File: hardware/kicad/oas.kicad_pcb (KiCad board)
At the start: 2 copper layers, 120 x 103.5 mm, 68 parts, among them J1 Phoenix_MSTBA_2,5/3-G-5,08 (2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, J10 Native-USB recovery (DNP), J2 SWD/UART Recovery (DNP), J3 JST SM06B-GHS-TB (SEN66 conne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, J4 1x5 P1.27mm header (HLK-LD241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, J5 ESP32 row A (pins 1..15, ante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, J6 ESP32 row B (pins 16..30, USB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, J7 MIKROE row A (mikroBUS pins 1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, J8 MIKROE row B (mikroBUS pins 9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, J9 JST SM04B-SRSS-TB (Qwiic / St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, Q1 AO3401A, U1 LM2596S-5.0, U2 TPS62933

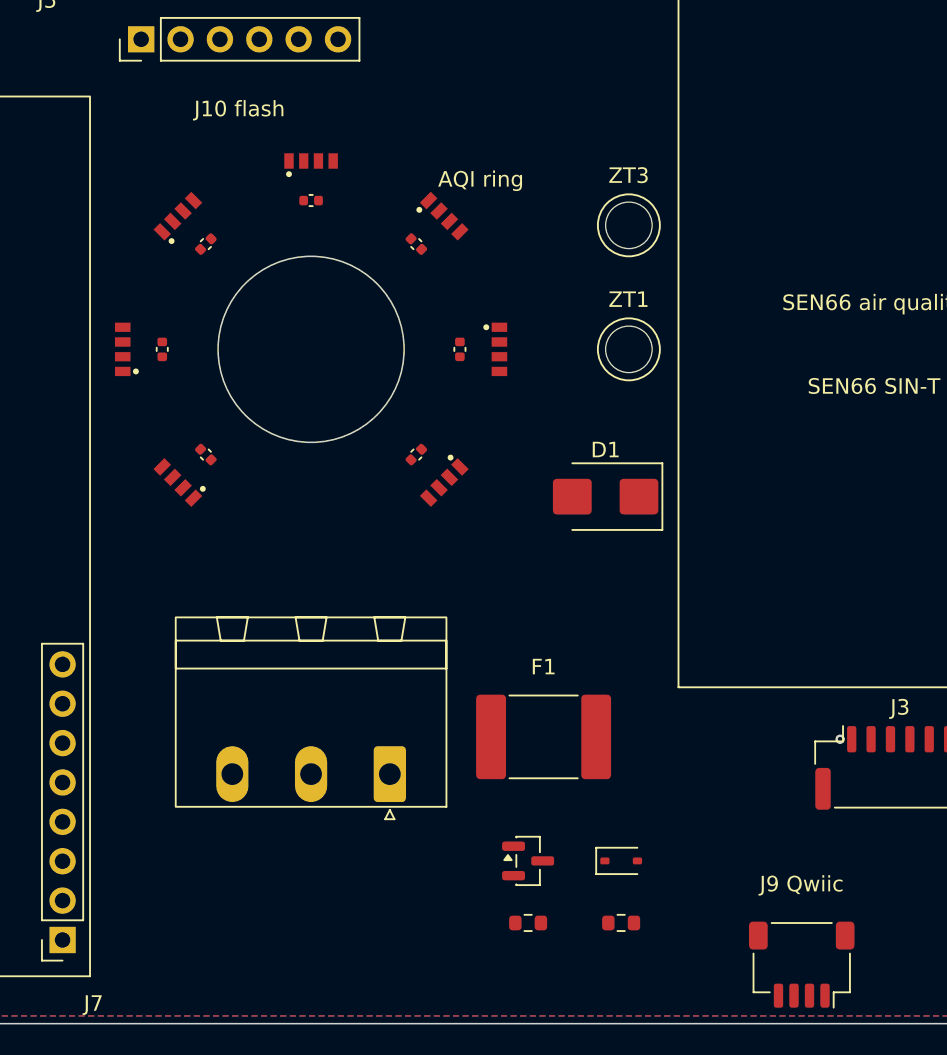
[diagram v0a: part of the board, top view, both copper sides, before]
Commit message: fix(boardgen): LED ring emission outward, F1 1812 downsize, J1 no-go zone
LED ring (SK6812-SIDE D11..D18):
- Flip rotation formula (270-theta) -> (90-theta) so emission face points
  radially OUTWARD from ring centre (was INWARD, hidden under cable hole).
- Bundle 3D STEP model from scottbez1/smartknob (Apache 2.0) so LEDs render
  in 3D. New libraries/oas.3dshapes/ with NOTICE.md for attribution.
- Add show_pin_labels option to gen_sk6812_side_pcb_footprint(); D11 gets
  vertical "Di"/"Gd" silk labels at pads 1/4 for visual orientation check
  during inspection.
- Per-LED radius overrides: D11/D15 R=11 (E-W axis symmetry), D12/D14
  R=16.5 (clear J1 mating plug), C21/C23 cap radial offset 2.6 mm (vs
  3.4 default) so caps sit OUTSIDE J1 plug no-go zone.

J1 (24V Phoenix terminal):
- Rotate Qwiic J9 180->0 (mating face faces south chord opening).
- Shift J1_PCB_Y +5 mm south to widen the plug clearance area.
- Add F.SilkS no-go rectangle (X=±8.73, Y=[+6.4,+21.5]) labelled "J1 PLUG"
  marking the area reserved for the mating plug. Component placement
  ensures nothing lies inside this rect.

F1 polyfuse:
- Downsize 2920 -> 1812 (Littelfuse 1812L075THDR, LCSC C262023) so the
  KiCad-stock R_1812_4532Metric.step can be used as the 3D body (CC-BY-SA
  + Design Exception, commitable to public repo). The stock 2920 footprint
  references a STEP file absent from KiCad 10 install.
- Add model_override parameter to _emit_stock_lib_footprint() helper to
  redirect (model ...) path when stock kicad_mod points at a missing file.

3D renders:
- Add 3 isometric views at 90/180/270 deg azimuth (in addition to existing
  iso = 0 deg) for full 360-deg visual review.

Layout follow-ups (all DRC clean):
- Move "J10 flash" silk text 3 mm south (D17 collision after radius bump).
- Increase MIKROE-2462 height/footprint half-extent entries to cover
  Fuse_1812_4532Metric footprint.
- Remove "AQI ring" board-level silk text (pads of D18 collided with
  the bbox after radius/rotation change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
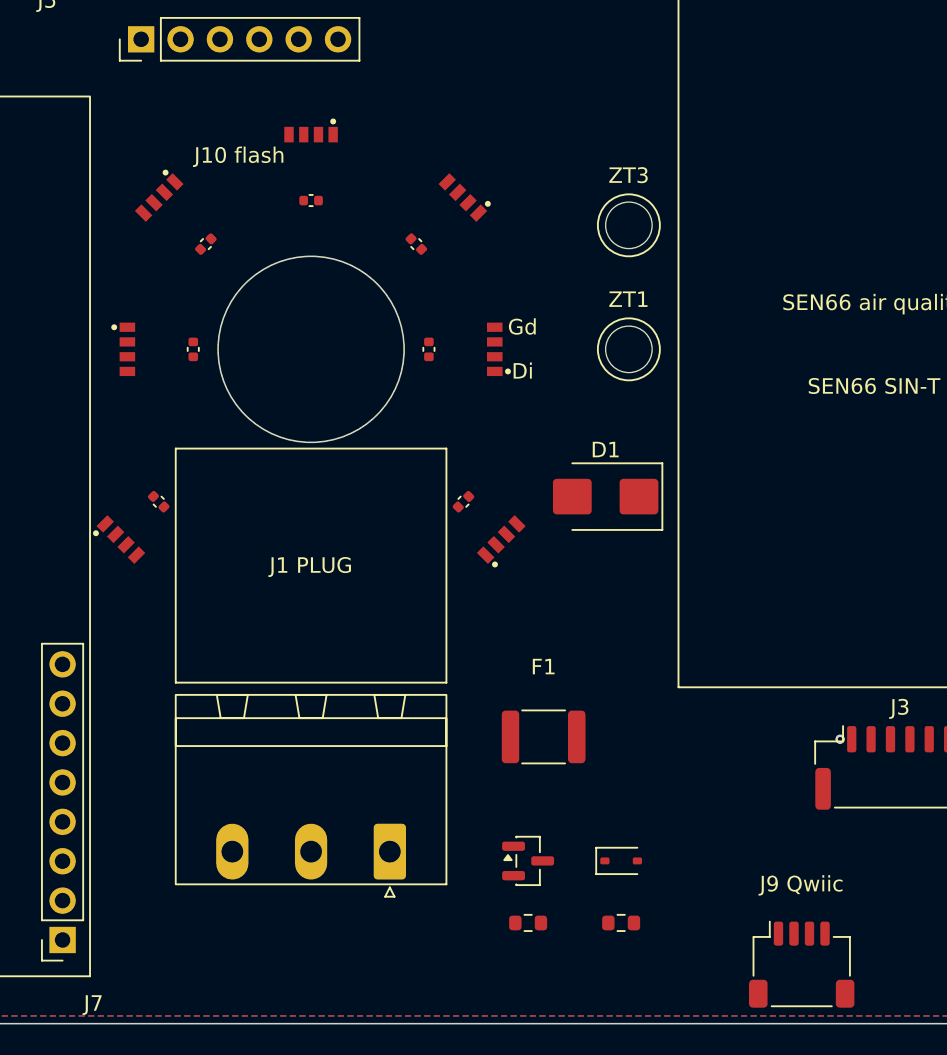
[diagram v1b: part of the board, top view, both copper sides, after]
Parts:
- F1: value MF-RHT075/60-2 -> 1812L075THDR; footprint Fuse:Fuse_2920_7451Metric -> Fuse:Fuse_1812_4532Metric
- moved J1 5.00 mm to (153.6, 137.4)
- moved C21 4.30 mm to (158.3, 114.8), turned to 45 degrees
- moved C23 4.30 mm to (138.7, 114.8), turned to 315 degrees
- moved D12 3.50 mm to (160.2, 116.7), turned to 45 degrees
- moved D14 3.50 mm to (136.8, 116.7), turned to 315 degrees
- moved C20 2.00 mm to (156.1, 105.0), turned to 90 degrees
- moved C24 2.00 mm to (140.9, 105.0), turned to 270 degrees
- moved D11 2.00 mm to (159.5, 105.0), turned to 90 degrees
- moved D15 2.00 mm to (137.5, 105.0), turned to 270 degrees
- turned C25 to 225 degrees
- turned C26 to 180 degrees
- turned C27 to 135 degrees
- turned D16 to 225 degrees
- turned D17 to 180 degrees
- turned D18 to 135 degrees
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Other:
- board text added: "J1 PLUG"
- board text removed: "AQI ring"

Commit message: fix(schematic): C9 non-polarized symbol + J2 label + doc drifts
Closes the remaining items from the 50-agent connectivity audit.

C9 (10 uF MLCC, Samsung CL21A106KAYNNNE — verified ceramic / X5R,
non-polarized) was drawn with Device:C_Polarized, implying a polarity
constraint the part does not have. Switch to Device:C. Connectivity is
unchanged: pin geometry is identical and the +3V3 / GND nets keep
their names.

J2 recovery header was labelled "SWD/UART Recovery" — the ESP32-C6 is
RISC-V and exposes no SWD; the header carries UART + EN + BOOT. Renamed
to "UART/Boot Recovery (DNP)" across BOTH the schematic generator and
the PCB footprint generator (the value string lives in each).

Doc drifts: CLAUDE.md F1 row corrected 2920L075/60MR (C207083) ->
1812L075THDR (C262023) to match the BOM / lcsc_mapping; _sch_mcu.py
GPIO16/17 comments corrected UART0 -> UART1.

29/29 build PASS — DRC 0, ERC 0, determinism OK.

Co-Authored-By: Claude Opus 4.7 <noreply@anthropic.com>
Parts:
- J2: value SWD/UART Recovery (DNP) -> UART/Boot Recovery (DNP)
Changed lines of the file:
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@@
 	(effects (font (size 1 1) (thickness 0.15)))
 )
-(property "Value" "SWD/UART Recovery (DNP)"
+(property "Value" "UART/Boot Recovery (DNP)"
 	(at 2.5 15 0)
 	(layer "F.Fab")

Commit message: fix(boardgen): move J9 to the C2 / RJ45-Ethernet case-wall opening
Physical fit-check of the AK-N-94 enclosure against the manufacturer
DXF showed J9 (Qwiic / Stemma QT) was placed behind a single Ø3.4 mm
round hole — nonsensical for a 4-pin cable connector. Relocate J9 from
the C5 opening to the C2 opening (the RJ45 / Ethernet jack cutout),
centred at PCB X = -8.95. CUTOUTS now emits only the populated C2
keepout zone; the "J9" cutout silk label is shortened and placed in
the silk corridor between the MIKROE NFC body and the J1 terminal block.

Co-Authored-By: Claude Opus 4.7 <noreply@anthropic.com>
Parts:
- moved J9 40.6 mm to (139.6, 144.7)
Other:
- board text added: "C2 15.7×16.3"
- board text added: "J9"
- board text removed: "C5 7.5×6.0"
- board text removed: "J9 Qwiic"
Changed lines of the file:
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@@
 )
 (gr_rect
-	(start 176.4 141.494)
-	(end 183.9 147.494)
+	(start 131.7 132.198)
+	(end 147.4 148.497798)
 	(stroke (width 0.1) (type solid))
 	(fill no)
 	(layer "Dwgs.User")
 )
-(gr_text "C5\n7.5×6.0"
-	(at 180.15 144.494)
+(gr_text "C2\n15.7×16.3"
+	(at 139.55 140.347899)
 	(layer "Dwgs.User")
 	(effects
@@
 (footprint "Connector_JST:JST_SH_SM04B-SRSS-TB_1x04-1MP_P1.00mm_Horizontal"
 	(layer "F.Cu")
-	(at 180.15 144.69 0)
+	(at 139.55 144.69 0)
 (property "Reference" "J9"
 	(at 0 -3.6 0)
@@
 )
 (gr_text "J9 GND"
-	(at 181.65 144.69 0)
+	(at 141.05 144.69 0)
 	(layer "F.Fab")
 	(effects
@@
 	)
 )
-(gr_text "J9 Qwiic"
-	(at 180.15 139.5 0)
+(gr_text "J9"
+	(at 137.64 139.5 0)
 	(layer "F.SilkS")
 	(effects
@@
 	(net_name "")
 	(layers "F.Cu" "B.Cu")
-	(name "Connector_Cutout_C5")
+	(name "Connector_Cutout_C2")
 	(hatch edge 0.508)
 	(connect_pads
@@
 	(polygon
 		(pts
-			(xy 176.4 141.494)
-			(xy 183.9 141.494)
-			(xy 183.9 147.494)
-			(xy 176.4 147.494)
+			(xy 131.7 132.198)
+			(xy 147.4 132.198)
+			(xy 147.4 148.497798)
+			(xy 131.7 148.497798)
 		)
 	)

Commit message: fix(boardgen): mirror J9 / C2 cutout to the +X side
The C2 RJ45 / Ethernet case-wall opening (which hosts the J9 Qwiic /
Stemma QT connector) was transcribed from a bottom-of-enclosure
manufacturer DXF without mirror correction, so it landed on the wrong
(-X / left) side of the board's vertical centerline.

Mirror-correct the C2 cutout X range about X=0 (now +1.1..+16.8),
recentre J9_PCB_X on the cutout midpoint (+8.95), and reposition the
board-level "J9" F.SilkS label into the clear silk corridor on the
+X side. Comments updated to reflect the bottom-view DXF correction.

Co-Authored-By: Claude Opus 4.7 <noreply@anthropic.com>
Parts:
- moved J9 17.9 mm to (157.4, 144.7)
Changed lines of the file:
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@@
 )
 (gr_rect
-	(start 131.7 132.198)
-	(end 147.4 148.497798)
+	(start 149.6 132.198)
+	(end 165.3 148.497798)
 	(stroke (width 0.1) (type solid))
 	(fill no)
@@
 )
 (gr_text "C2\n15.7×16.3"
-	(at 139.55 140.347899)
+	(at 157.45 140.347899)
 	(layer "Dwgs.User")
 	(effects
@@
 (footprint "Connector_JST:JST_SH_SM04B-SRSS-TB_1x04-1MP_P1.00mm_Horizontal"
 	(layer "F.Cu")
-	(at 139.55 144.69 0)
+	(at 157.45 144.69 0)
 (property "Reference" "J9"
 	(at 0 -3.6 0)
@@
 )
 (gr_text "J9 GND"
-	(at 141.05 144.69 0)
+	(at 158.95 144.69 0)
 	(layer "F.Fab")
 	(effects
@@
 )
 (gr_text "J9"
-	(at 137.64 139.5 0)
+	(at 158.9 139.5 0)
 	(layer "F.SilkS")
 	(effects
@@
 	(polygon
 		(pts
-			(xy 131.7 132.198)
-			(xy 147.4 132.198)
-			(xy 147.4 148.497798)
-			(xy 131.7 148.497798)
+			(xy 149.6 132.198)
+			(xy 165.3 132.198)
+			(xy 165.3 148.497798)
+			(xy 149.6 148.497798)
 		)
 	)

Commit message: feat(sw1): add SW1 side-actuated tactile push-button (v0.42)
Adds the C&K PTS645VK392LFS right-angle THT push-button on ESP32-C6
GPIO 1, mounted in the AK-N-94 USB-C case-wall opening. Short press
cycles the LED ring brightness, long press restarts the MCU.

Hardware: GPIO 1 -> BTN net, new USBC cutout + SW1 placement constants,
Switch:SW_Push stock symbol on the IO sheet, verbatim-stock PTS645
footprint, inter-sheet BTN wiring (IO -> MCU). SW1 added to
THT_REFERENCES; DRC EXPECTED_UNCONNECTED 88 -> 89 (BTN ratsnest routed
in the pending routing rework).

Firmware: new packages/buttons.yaml (GPIO1 binary_sensor + brightness-
cycle script), wired into oas.yaml.

All 29 pipeline stages PASS; boardgen output deterministic.

Co-Authored-By: Claude Opus 4.7 <noreply@anthropic.com>
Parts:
- added SW1: C&K PTS645VK392LFS, Button_Switch_THT:SW_Tactile_SPST_Angled_PTS645Vx39-2LFS, F.Cu at (143.5, 146.0)
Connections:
- J5 pad 8: unconnected-(J5-Pin_8-Pad8) -> /IO/BTN
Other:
- board text added: "SW1"
- board text added: "USBC 11.0×16.3"

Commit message: feat(silkscreen): derive per-pin + polarity labels, board-id block (v0.43)
Silkscreen review + extension so every per-pin / polarity mark is
derived from the actual footprint placement instead of being hand-typed.

- New connector pin maps (J1/J2/J9/J10) in boardgen/_project.py as the
  single source of truth; _sch_mcu.py now imports J2_PIN_MAP instead of
  duplicating it, so silk labels can never drift from the netlist.
- _pin_labels() helper transforms footprint-local pad coordinates by the
  same rotation matrix KiCad applies to the placed footprint, so per-pin
  label positions are derived, not hand-coordinated.
- J2 per-pin labels added (were missing entirely); J1/J10 per-pin now
  sourced from the pin maps. Per-pin signal labels stay on F.Fab where
  the crowded layout / silk_min_text_height rule blocks clean F.SilkS.
- End-pin numbers (pin 1 + last pin) added on F.SilkS for ESP32 J5/J6,
  MIKROE-2462 J7/J8 and LD2410 J4, placed just outside each module body.
- "J10 flash" designator moved east of the pad row (was 7.5 mm south).
- Board-id block (name + version) relocated to the F.SilkS pocket under
  J3; version read from OAS_VERSION_LINE, bumped v0.40 -> v0.43; the
  repo URL is dropped (too wide for the pocket at silk min text height).
- New pipeline stage 21 check_polarity_silk fails the build if any
  orientation-critical part (D1-D3, Q1, U1/U2, C1/C4, D11-D18) loses
  its pad-1 + F.SilkS polarity primitive. Audit confirms all polarity
  silk is stock-footprint-derived (rotates with placement) or computed
  from pad geometry (SK6812 LEDs) - no hand-drawn approximations.

30/30 pipeline stages PASS; DRC 0, ERC 0, determinism bit-identical.

Co-Authored-By: Claude Opus 4.7 <noreply@anthropic.com>
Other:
- board text added: "1"
- board text added: "15"
- board text added: "5"
- board text added: "8"
- board text added: "RX"
- board text added: "TX"
- board text added: "v0.43"
- board text removed: "OAS v0.40"
- board text removed: "github.com/HubertCiebiada/open-ambient-sensor"
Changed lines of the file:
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@@
 )
 (gr_text "Open Ambient Sensor"
-	(at 144.5 135 0)
-	(layer "F.Fab")
-	(effects
-		(font (size 1 1) (thickness 0.15))
-	)
-)
-(gr_text "OAS  v0.40"
-	(at 144.5 138 0)
-	(layer "F.Fab")
-	(effects
-		(font (size 1 1) (thickness 0.15))
-	)
-)
-(gr_text "github.com/HubertCiebiada/open-ambient-sensor"
-	(at 144.5 141 0)
-	(layer "F.Fab")
-	(effects
-		(font (size 0.9 0.9) (thickness 0.15))
+	(at 189 138.5 0)
+	(layer "F.SilkS")
+	(effects
+		(font (size 1 1) (thickness 0.15))
+	)
+)
+(gr_text "v0.43"
+	(at 189 142 0)
+	(layer "F.SilkS")
+	(effects
+		(font (size 1 1) (thickness 0.15))
 	)
 )
@@
 	)
 )
+(gr_text "+3V3"
+	(at 97.2 97 0)
+	(layer "F.Fab")
+	(effects
+		(font (size 0.8 0.8) (thickness 0.15))
+	)
+)
+(gr_text "GND"
+	(at 97.2 99.54 0)
+	(layer "F.Fab")
+	(effects
+		(font (size 0.8 0.8) (thickness 0.15))
+	)
+)
+(gr_text "TX"
+	(at 97.2 102.08 0)
+	(layer "F.Fab")
+	(effects
+		(font (size 0.8 0.8) (thickness 0.15))
+	)
+)
+(gr_text "RX"
+	(at 97.2 104.62 0)
+	(layer "F.Fab")
+	(effects
+		(font (size 0.8 0.8) (thickness 0.15))
+	)
+)
+(gr_text "EN"
+	(at 97.2 107.16 0)
+	(layer "F.Fab")
+	(effects
+		(font (size 0.8 0.8) (thickness 0.15))
+	)
+)
+(gr_text "BOOT"
+	(at 97.2 109.7 0)
+	(layer "F.Fab")
+	(effects
+		(font (size 0.8 0.8) (thickness 0.15))
+	)
+)
 (gr_text "J9 GND"
 	(at 158.95 144.69 0)
@@
 )
 (gr_text "J10 flash"
-	(at 143.89 92.5 0)
+	(at 155.44 85 0)
 	(layer "F.SilkS")
 	(effects
@@
 	(layer "F.SilkS")
 	(effects
+		(font (size 1 1) (thickness 0.15))
+	)
+)
+(gr_text "1"
+	(at 126.11 81.93 0)
+	(layer "F.SilkS")
+	(effects
+		(font (size 1 1) (thickness 0.15))
+	)
+)
+(gr_text "15"
+	(at 161.67 81.93 0)
+	(layer "F.SilkS")
+	(effects
+		(font (size 1 1) (thickness 0.15))
+	)
+)
+(gr_text "1"
+	(at 126.11 53.27 0)
+	(layer "F.SilkS")
+	(effects
+		(font (size 1 1) (thickness 0.15))
+	)
+)
+(gr_text "15"
+	(at 161.67 53.27 0)
+	(layer "F.SilkS")
+	(effects
+		(font (size 1 1) (thickness 0.15))
+	)
+)
+(gr_text "1"
+	(at 135.37 143.1 0)
+	(layer "F.SilkS")
+	(effects
+		(font (size 1 1) (thickness 0.15))
+	)
+)
+(gr_text "8"
+	(at 135.37 125.32 0)
+	(layer "F.SilkS")
+	(effects
+		(font (size 1 1) (thickness 0.15))
+	)
+)
+(gr_text "1"
+	(at 106.71 143.1 0)
+	(layer "F.SilkS")
+	(effects
+		(font (size 1 1) (thickness 0.15))
+	)
+)
+(gr_text "8"
+	(at 106.71 125.32 0)
+	(layer "F.SilkS")
+	(effects
+		(font (size 1 1) (thickness 0.15))
+	)
+)
+(gr_text "1"
+	(at 103.76 126.95 0)
+	(layer "F.SilkS")
+	(effects
+		(font (size 1 1) (thickness 0.15))
+	)
+)
+(gr_text "5"
+	(at 98.68 126.95 0)
+	(layer "F.SilkS")
+	(effects
